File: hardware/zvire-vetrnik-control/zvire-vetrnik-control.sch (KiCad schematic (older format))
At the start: 87 parts, among them J1 Conn_01x20_Male, J10 Conn_01x04, J11 Conn_01x03_Male, J12 Conn_01x08_Male, J13 RJ45, J14 Conn_01x04, J15 Conn_01x03, J16 Conn_01x04, J17 Conn_01x04, J18 Conn_01x03, J19 Conn_01x03, J2 Conn_01x04, J20 Conn_01x04, J21 Conn_01x04, J3 Conn_01x03, J4 Conn_02x04_Odd_Even, J5 Conn_02x04_Odd_Even, J6 Conn_02x04_Odd_Even, J7 Conn_01x20_Male, J8 Screw_Terminal_01x02, J9 Conn_01x03, Q1 BC857, Q2 BC847, Q3 BC847, Q4 BC847, Q5 BC847, Q6 BSS138, Q7 BSS138, Q8 BSS138, SW1 SW_Push, SW2 SW_Push, U1 LTV-817S, U2 YAAJ_WeAct_BlackPill_Part_Like, U3 MX25L8006EM1I-12G, U4 WIZ850io

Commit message: [hardware] Design PCB for control board
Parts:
- removed C13: 100n, Capacitor_SMD:C_1206_3216Metric_Pad1.33x1.80mm_HandSolder, symbol Device:C
- removed J12: Conn_01x08_Male, Connector_PinHeader_2.54mm:PinHeader_1x08_P2.54mm_Vertical, symbol Connector:Conn_01x08_Male
- removed J13: RJ45, Connector_RJ:RJ45_Amphenol_54602-x08_Horizontal, symbol Connector:RJ45
- removed J18, J19: Conn_01x03, Connector_Molex:Molex_KK-254_AE-6410-03A_1x03_P2.54mm_Vertical, symbol Connector_Generic:Conn_01x03
- added J12, J13, J14: Conn_02x04_Odd_Even, Connector_PinHeader_2.54mm:PinHeader_2x04_P2.54mm_Vertical, symbol Connector_Generic:Conn_02x04_Odd_Even
- added R22, R25: 0, Resistor_SMD:R_1206_3216Metric_Pad1.30x1.75mm_HandSolder, symbol Device:R
- renumbered C11 to C10, C12 to C11, C10 to C12, C14 to C13, C15 to C14, J14 to J15, J15 to J18, J20 to J19, J21 to J20, Q7 to Q5, Q8 to Q6, Q5 to Q7, Q6 to Q8, R21 to R18, R22 to R19, R24 to R20, R25 to R21, R18 to R23, R19 to R24, R20 to R26, R23 to R27
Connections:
- net +3V3: now also J9.3 (Pin_3); no longer J9.1 (Pin_1)
- net +5V: now also J18.3 (Pin_3); no longer J18.1 (Pin_1)
- net ADC_NTC2: now also J9.1 (Pin_1); no longer J9.3 (Pin_3)
- net GND: now also J18.1 (Pin_1); no longer J18.3 (Pin_3)
- net MOSI: now also R25.2; no longer U4.3 (MOSI)
- net PA10: now also R22.2; no longer J15.2 (Pin_2)
- net at U1.2: now also J8.2 (Pin_2); no longer J8.1 (Pin_1)
- net at R7.2: now also J8.1 (Pin_1); no longer J8.2 (Pin_2)
- net BP1 renamed PB1
- net BP2 renamed PB2
- new net: J15.2 (Pin_2), R22.1
- new net: R25.1, U4.3 (MOSI)
- new net: J12.1 (Pin_1), J12.3 (Pin_3), J12.5 (Pin_5), J12.7 (Pin_7)
- new net: J12.2 (Pin_2), J12.4 (Pin_4), J12.6 (Pin_6), J12.8 (Pin_8)
- new net: J13.1 (Pin_1), J13.3 (Pin_3), J13.5 (Pin_5), J13.7 (Pin_7)
- new net: J13.2 (Pin_2), J13.4 (Pin_4), J13.6 (Pin_6), J13.8 (Pin_8)
- new net: J14.1 (Pin_1), J14.3 (Pin_3), J14.5 (Pin_5), J14.7 (Pin_7)
- new net: J14.2 (Pin_2), J14.4 (Pin_4), J14.6 (Pin_6), J14.8 (Pin_8)
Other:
- note removed: "5V onewire should be preferred"
- note removed: "RJ45 CONN\nFOR FUTURE USE"
- note removed: "TODO\n- verify Ethernet footprint"
- moved on the sheet: BZ1, C12, H1, H2, H3, H4, J15, J18, JP2, Q7, Q8, R23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

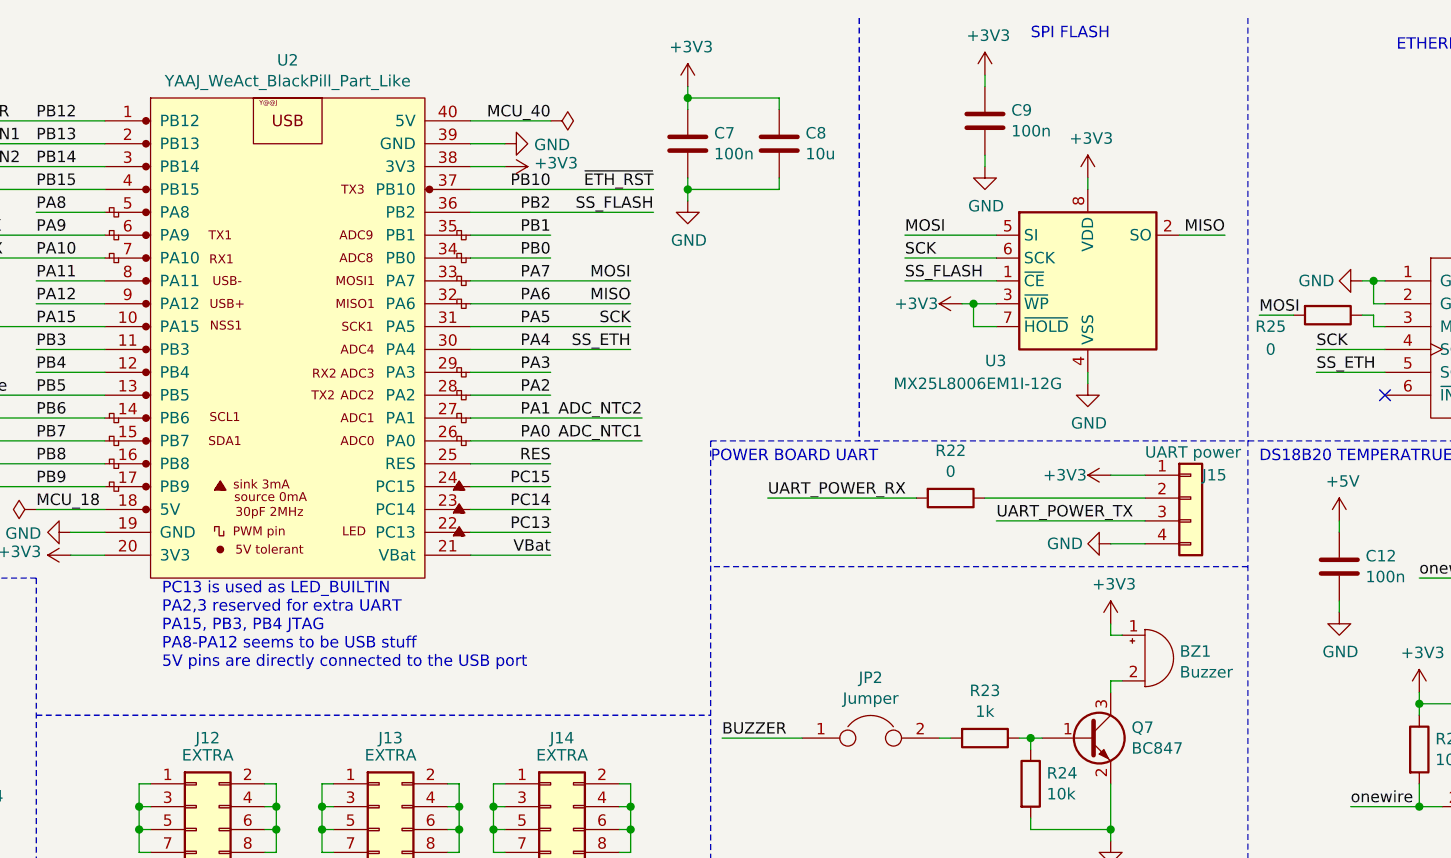
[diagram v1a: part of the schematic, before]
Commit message: [control] Use PB1 as SPIflash SS instead of PB2
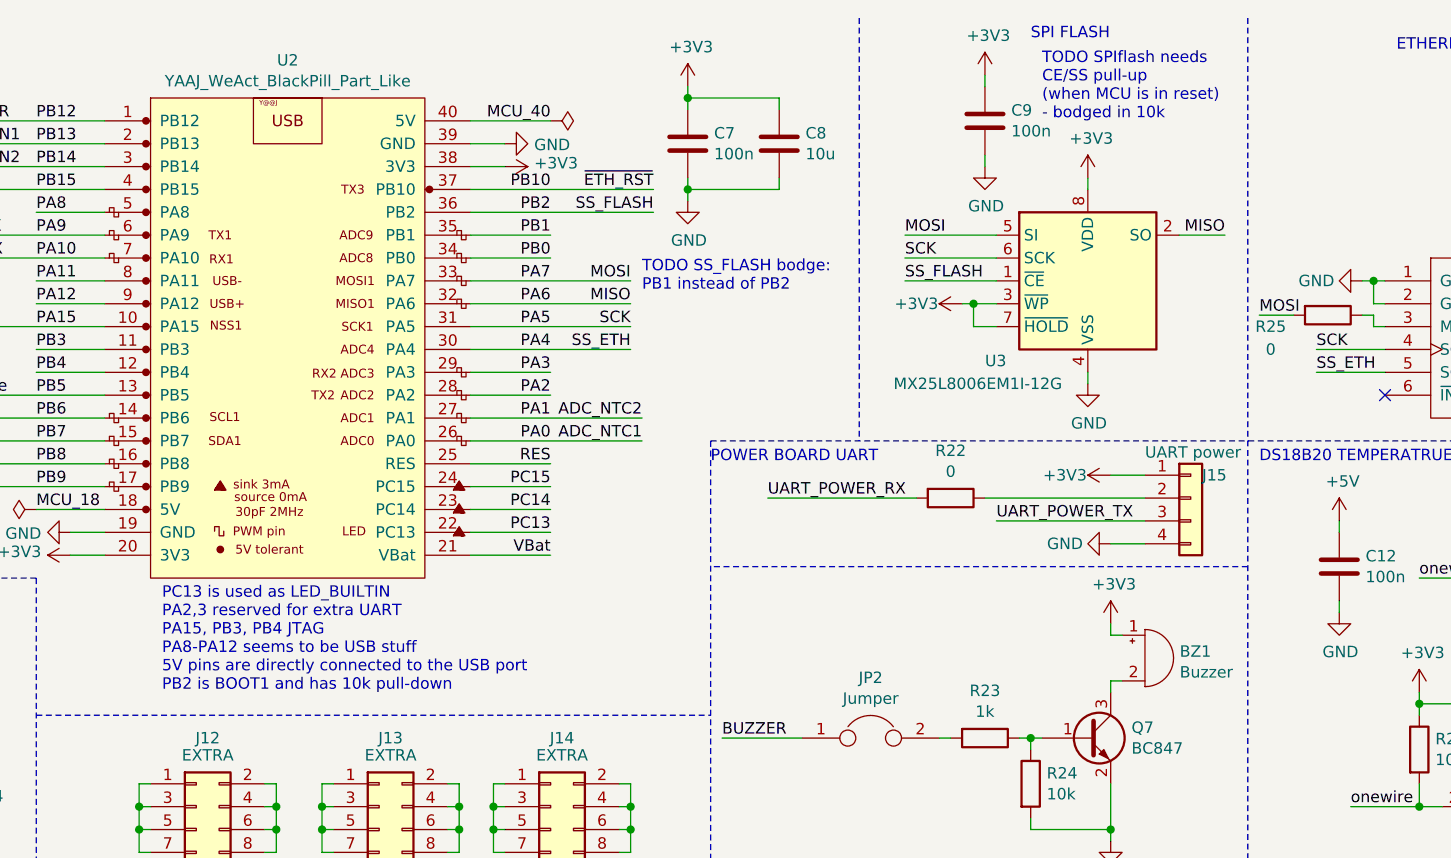
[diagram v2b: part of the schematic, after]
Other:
- note added: "PC13 is used as LED_BUILTIN\nPA2,3 reserved for extra UART\nPA15, PB3, PB4 JTAG\nPA8-PA12 seems to be USB stuff\n5V pins are directly connected to the USB port\nPB2 is BOOT1 and has 10k pull-down"
- note added: "TODO SPIflash needs\nCE/SS pull-up\n(when MCU is in reset)\n- bodged in 10k"
- note added: "TODO SS_FLASH bodge:\nPB1 instead of PB2"
- note removed: "PC13 is used as LED_BUILTIN\nPA2,3 reserved for extra UART\nPA15, PB3, PB4 JTAG\nPA8-PA12 seems to be USB stuff\n5V pins are directly connected to the USB port"
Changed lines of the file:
@@
 Wire Wire Line
 	3500 2300 4200 2300
-Text Notes 4450 3300 0    50   ~ 0
-PC13 is used as LED_BUILTIN\nPA2,3 reserved for extra UART\nPA15, PB3, PB4 JTAG\nPA8-PA12 seems to be USB stuff\n5V pins are directly connected to the USB port
+Text Notes 4450 3400 0    50   ~ 0
+PC13 is used as LED_BUILTIN\nPA2,3 reserved for extra UART\nPA15, PB3, PB4 JTAG\nPA8-PA12 seems to be USB stuff\n5V pins are directly connected to the USB port\nPB2 is BOOT1 and has 10k pull-down
 Text Label 3500 2100 0    50   ~ 0
 onewire
@@
 Wire Wire Line
 	6500 4000 6500 4100
+Text Notes 8300 900  0    50   ~ 0
+TODO SPIflash needs\nCE/SS pull-up\n(when MCU is in reset)\n- bodged in 10k
+Text Notes 6550 1650 0    50   ~ 0
+TODO SS_FLASH bodge:\nPB1 instead of PB2
 $EndSCHEMATC

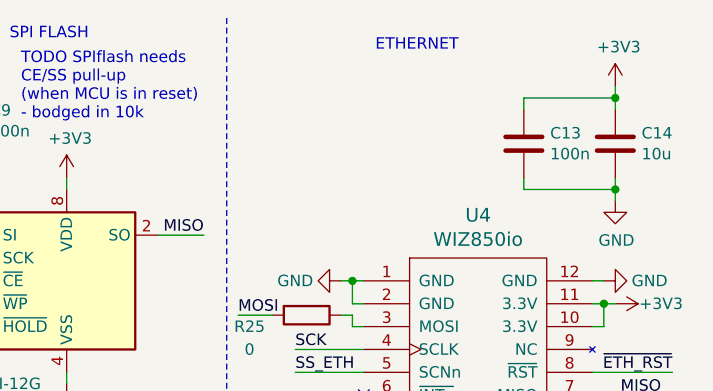
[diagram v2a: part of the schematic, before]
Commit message: [hardware] [control] Fix Ethernet reset by EMI
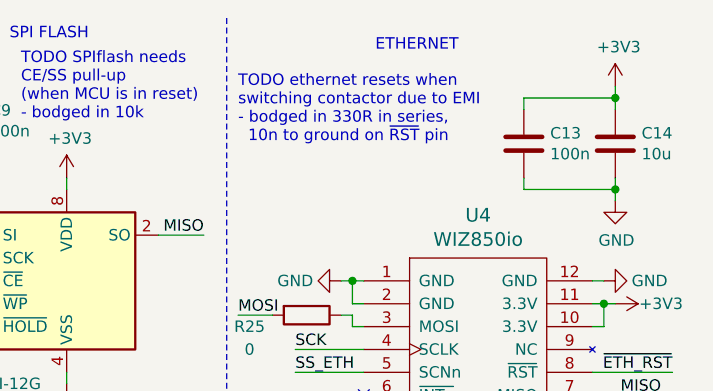
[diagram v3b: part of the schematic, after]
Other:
- note added: "TODO ethernet resets when\nswitching contactor due to EMI\n- bodged in 330R in series,\n 10n to ground on ~RST~ pin"
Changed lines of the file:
@@
 Text Notes 6550 1650 0    50   ~ 0
 TODO SS_FLASH bodge:\nPB1 instead of PB2
+Text Notes 9250 1000 0    50   ~ 0
+TODO ethernet resets when\nswitching contactor due to EMI\n- bodged in 330R in series,\n  10n to ground on ~RST~ pin
 $EndSCHEMATC

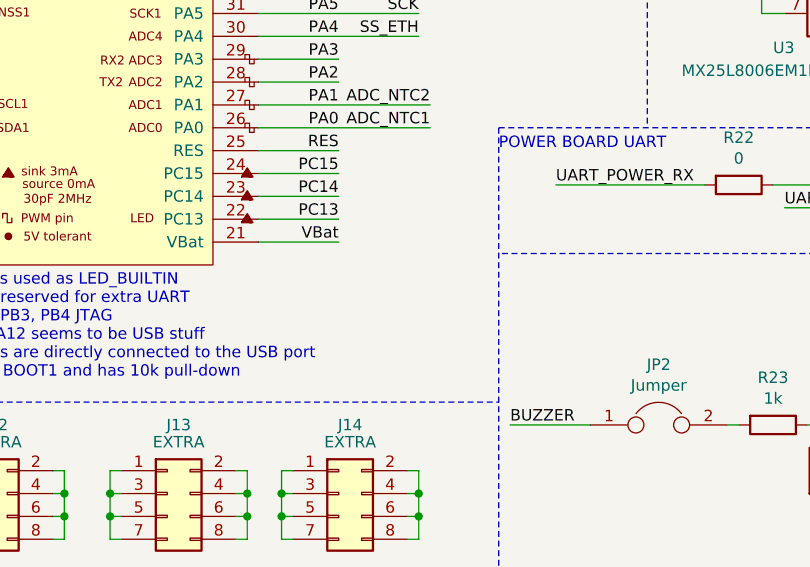
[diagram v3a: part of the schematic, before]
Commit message: [control] Sense contactor state and handle e-stop
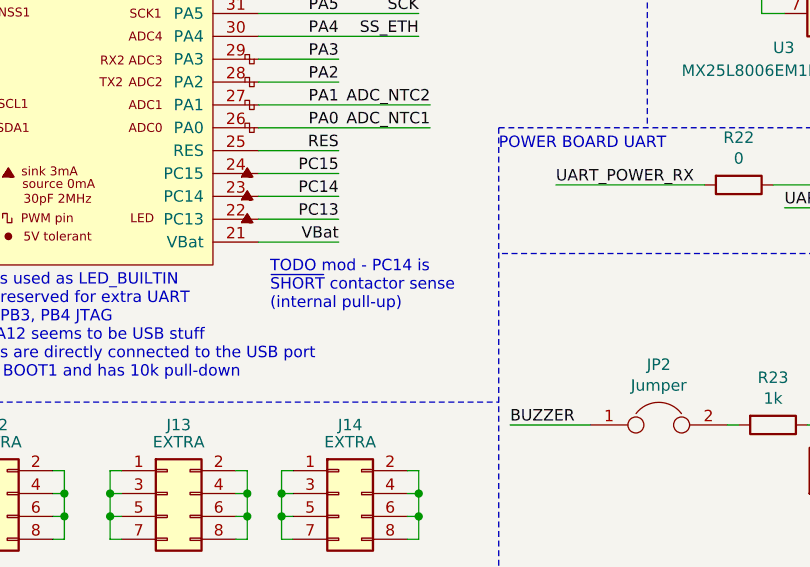
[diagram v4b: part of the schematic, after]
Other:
- note added: "TODO mod - PC14 is\n~SHORT~ contactor sense\n(internal pull-up)"
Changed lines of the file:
@@
 Text Notes 9250 1000 0    50   ~ 0
 TODO ethernet resets when\nswitching contactor due to EMI\n- bodged in 330R in series,\n  10n to ground on ~RST~ pin
+Text Notes 5850 3100 0    50   ~ 0
+TODO mod - PC14 is\n~SHORT~ contactor sense\n(internal pull-up)
 $EndSCHEMATC
